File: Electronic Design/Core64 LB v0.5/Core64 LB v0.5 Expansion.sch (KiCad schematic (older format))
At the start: 21 parts, among them J2 HEADER_11-PIN_0.1, J5 HEADER_8-PIN_0.1, J6 HEADER_8-PIN_0.1, U5 74HC238, U8 Adafruit_3.2_TFT_1743, X1 QWIIC, X2 Header_9-PIN_0.1, X3 SAO_conn_SFH11-NBPC-D03-ST-BK, X4 SSW-104-22-L-S-VS

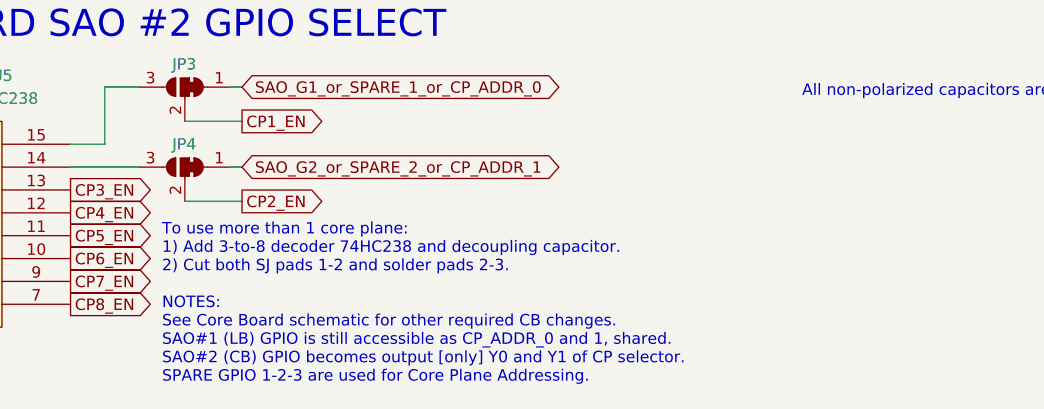
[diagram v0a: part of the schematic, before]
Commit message: Connect row-col-0 to analog inputs for self-test mode
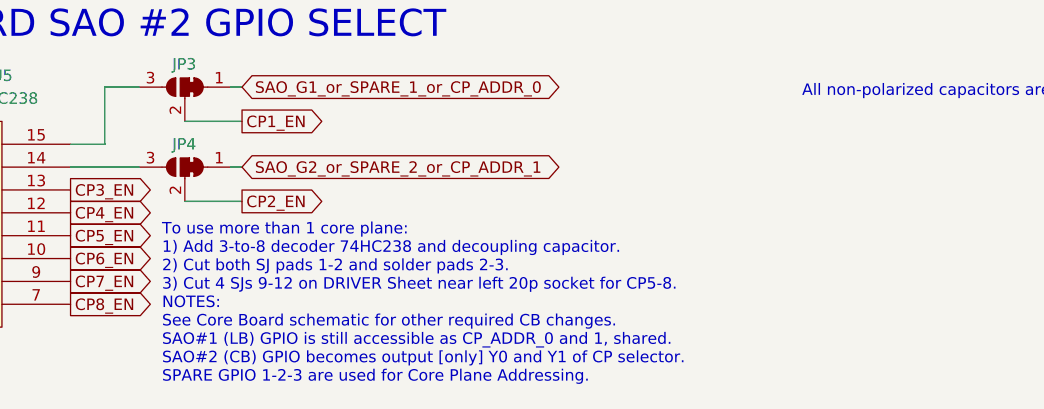
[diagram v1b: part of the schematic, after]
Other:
- note added: "To use more than 1 core plane:\n1) Add 3-to-8 decoder 74HC238 and decoupling capacitor.\n2) Cut both SJ pads 1-2 and solder pads 2-3.\n3) Cut 4 SJs 9-12 on DRIVER Sheet near left 20p socket for CP5-8.\nNOTES:\nSee Core Board schematic for other required CB changes.\nSAO#1 (LB) GPIO is still accessible as CP_ADDR_0 and 1, shared.\nSAO#2 (CB) GPIO becomes output [only] Y0 and Y1 of CP selector.\nSP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"
- note removed: "To use more than 1 core plane:\n1) Add 3-to-8 decoder 74HC238 and decoupling capacitor.\n2) Cut both SJ pads 1-2 and solder pads 2-3.\n\nNOTES:\nSee Core Board schematic for other required CB changes.\nSAO#1 (LB) GPIO is still accessible as CP_ADDR_0 and 1, shared.\nSAO#2 (CB) GPIO becomes output [only] Y0 and Y1 of CP selector.\nSPARE GPIO 1-2-3 are used for Core Plane Addressing."
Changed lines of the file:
@@
 EVERYTHING ON THIS SHEET IS USER-PROVIDED OPTIONAL ADD-ONS
 Text Notes 3500 8000 0    50   ~ 0
-To use more than 1 core plane:\n1) Add 3-to-8 decoder 74HC238 and decoupling capacitor.\n2) Cut both SJ pads 1-2 and solder pads 2-3.\n\nNOTES:\nSee Core Board schematic for other required CB changes.\nSAO#1 (LB) GPIO is still accessible as CP_ADDR_0 and 1, shared.\nSAO#2 (CB) GPIO becomes output [only] Y0 and Y1 of CP selector.\nSPARE GPIO 1-2-3 are used for Core Plane Addressing.
+To use more than 1 core plane:\n1) Add 3-to-8 decoder 74HC238 and decoupling capacitor.\n2) Cut both SJ pads 1-2 and solder pads 2-3.\n3) Cut 4 SJs 9-12 on DRIVER Sheet near left 20p socket for CP5-8.\nNOTES:\nSee Core Board schematic for other required CB changes.\nSAO#1 (LB) GPIO is still accessible as CP_ADDR_0 and 1, shared.\nSAO#2 (CB) GPIO becomes output [only] Y0 and Y1 of CP selector.\nSPARE GPIO 1-2-3 are used for Core Plane Addressing.
 Wire Wire Line
 	3600 6850 3850 6850

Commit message: LB layout redlines
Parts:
- U5: footprint Digikey:TSSOP-16-1EP_W4.40mm -> Digikey:TSSOP-16-W4.40mm
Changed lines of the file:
@@
 F 0 "U5" H 2800 7650 50  0000 C CNN
 F 1 "74HC238" H 2800 7550 50  0000 C CNN
-F 2 "Digikey:TSSOP-16-1EP_W4.40mm" H 2550 7150 50  0001 C CNN
+F 2 "Digikey:TSSOP-16-W4.40mm" H 2550 7150 50  0001 C CNN
 F 3 "" H 2550 7150 50  0001 C CNN
 	1    2550 7150

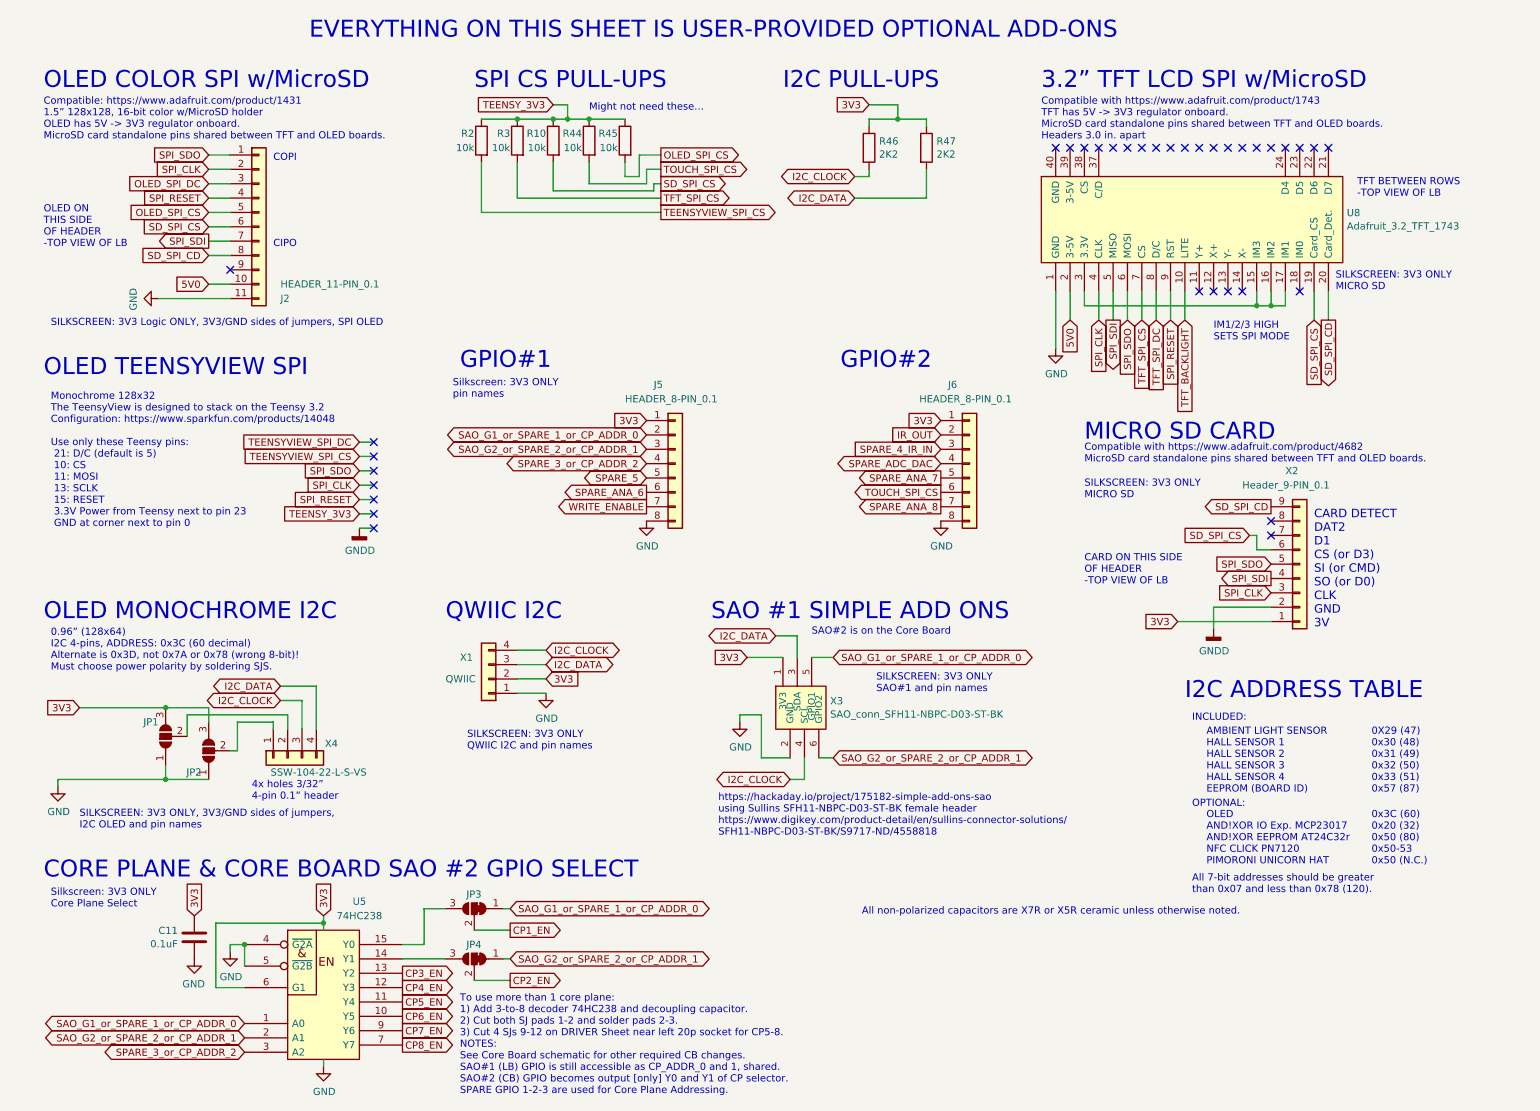
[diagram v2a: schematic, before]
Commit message: Update schematic battery and LiPo charger notes, move SD_CD from ANA_6 to SPARE_3, schematic red lines
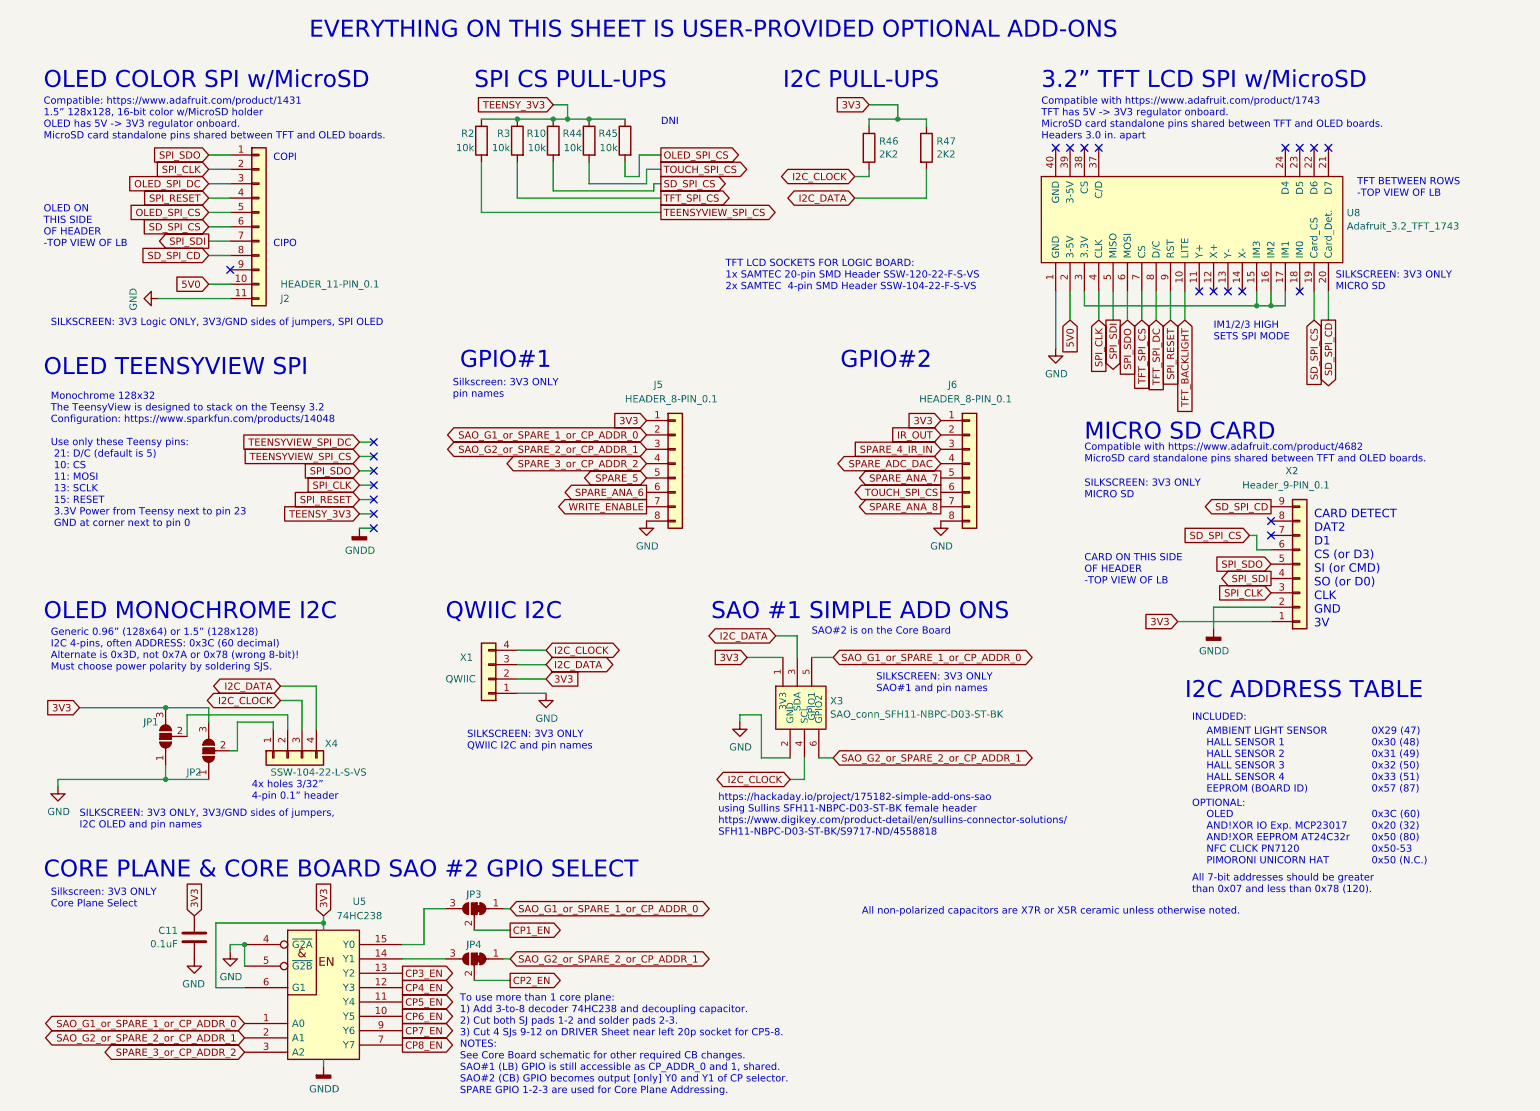
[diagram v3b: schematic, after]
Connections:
- net GNDD is gone; now on net GND: X2.2 (Pin_2)
- no-connect marks 35 -> 23
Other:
- note added: "DNI"
- note added: "Generic 0.96” (128x64) or 1.5” (128x128)\nI2C 4-pins, often ADDRESS: 0x3C (60 decimal)\nAlternate is 0x3D, not 0x7A or 0x78 (wrong 8-bit)!\nMust choose power polarity by soldering SJS."
- note added: "TFT LCD SOCKETS FOR LOGIC BOARD:\n1x SAMTEC 20-pin SMD Header SSW-120-22-F-S-VS\n2x SAMTEC 4-pin SMD Header SSW-104-22-F-S-VS"
- note removed: "0.96” (128x64)\nI2C 4-pins, ADDRESS: 0x3C (60 decimal)\nAlternate is 0x3D, not 0x7A or 0x78 (wrong 8-bit)!\nMust choose power polarity by soldering SJS."
- note removed: "Might not need these…"
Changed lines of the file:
@@
 Date "2021-02-04"
 Rev "0.5"
-Comp "www.Core64.io"
-Comment1 "Work in progress"
-Comment2 "Andy Geppert"
+Comp "Concept and design by Andy Geppert @ www.MachineIdeas.com"
+Comment1 "Visit www.Core64.io for information on assembly and optional features."
+Comment2 "*** Work in progress ***"
 Comment3 ""
-Comment4 ""
+Comment4 "All non-polarized capacitors are X7R or X5R ceramic unless otherwise noted."
 $EndDescr
 Text Notes 600  6500 0    118  ~ 0
@@
 	2200 5400 2200 5450
 Text Notes 650  5050 0    50   ~ 0
-0.96” (128x64)\nI2C 4-pins, ADDRESS: 0x3C (60 decimal)\nAlternate is 0x3D, not 0x7A or 0x78 (wrong 8-bit)!\nMust choose power polarity by soldering SJS.
-$Comp
-L badgelife_shitty_addon_v169bis:SAO_conn_SFH11-NBPC-D03-ST-BK X3
-U 1 1 5E88FF30
-P 5900 5250
-F 0 "X3" H 6079 5247 50  0000 L CNN
-F 1 "SAO_conn_SFH11-NBPC-D03-ST-BK" H 6079 5154 50  0000 L CNN
-F 2 "badgelife_sao_v169bis:Badgelife-SAOv169-BADGE-2x3" H 5900 5450 50  0001 C CNN
-F 3 "" H 5900 5450 50  0001 C CNN
-	1    5900 5250
-	1    0    0    -1
-$EndComp
+Generic 0.96” (128x64) or 1.5” (128x128)\nI2C 4-pins, often ADDRESS: 0x3C (60 decimal)\nAlternate is 0x3D, not 0x7A or 0x78 (wrong 8-bit)!\nMust choose power polarity by soldering SJS.
 Text GLabel 5500 4950 0    50   Input ~ 0
 3V3
@@
 	1    0    0    -1
 $EndComp
-$Comp
-L Connector_Generic:Conn_01x09 X2
-U 1 1 5EAA1F67
-P 9350 4300
-AR Path="/5EA63449/5EAA1F67" Ref="X2"  Part="1"
-AR Path="/5EAA1F67" Ref="X?"  Part="1"
-F 0 "X2" H 9250 3650 50  0000 L CNN
-F 1 "Header_9-PIN_0.1" H 8950 3750 50  0000 L CNN
-F 2 "Connector_PinSocket_2.54mm:PinSocket_1x09_P2.54mm_Vertical" H 9350 4300 50  0001 C CNN
-F 3 "~" H 9350 4300 50  0001 C CNN
-	1    9350 4300
-	1    0    0    1
-$EndComp
 Wire Wire Line
 	8750 4750 8750 4600
@@
 Text Notes 6300 6750 0    50   ~ 0
 All non-polarized capacitors are X7R or X5R ceramic unless otherwise noted.
-$Comp
-L power:GND #PWR?
-U 1 1 5F702794
-P 2550 7800
-AR Path="/5E755787/5F702794" Ref="#PWR?"  Part="1"
-AR Path="/5EA63449/5F702794" Ref="#PWR0126"  Part="1"
-F 0 "#PWR0126" H 2550 7550 50  0001 C CNN
-F 1 "GND" H 2555 7625 50  0000 C CNN
-F 2 "" H 2550 7800 50  0001 C CNN
-F 3 "" H 2550 7800 50  0001 C CNN
-	1    2550 7800
-	1    0    0    -1
-$EndComp
 Text GLabel 2550 6750 1    50   Input ~ 0
 3V3
@@
 Wire Wire Line
 	2000 7100 2000 6950
-Text GLabel 3850 6850 2    50   Output ~ 0
-CP1_EN
 $Comp
 L power:GND #PWR?
@@
 Text GLabel 2000 7600 0    50   BiDi ~ 0
 SAO_G2_or_SPARE_2_or_CP_ADDR_1
-Text GLabel 3850 6700 2    50   BiDi ~ 0
-SAO_G1_or_SPARE_1_or_CP_ADDR_0
 Text GLabel 3850 7050 2    50   BiDi ~ 0
 SAO_G2_or_SPARE_2_or_CP_ADDR_1
@@
 Text Notes 3500 8000 0    50   ~ 0
 To use more than 1 core plane:\n1) Add 3-to-8 decoder 74HC238 and decoupling capacitor.\n2) Cut both SJ pads 1-2 and solder pads 2-3.\n3) Cut 4 SJs 9-12 on DRIVER Sheet near left 20p socket for CP5-8.\nNOTES:\nSee Core Board schematic for other required CB changes.\nSAO#1 (LB) GPIO is still accessible as CP_ADDR_0 and 1, shared.\nSAO#2 (CB) GPIO becomes output [only] Y0 and Y1 of CP selector.\nSPARE GPIO 1-2-3 are used for Core Plane Addressing.
-Wire Wire Line
-	3600 6850 3850 6850
-Wire Wire Line
-	3800 6700 3850 6700
-$Comp
-L Jumper:SolderJumper_3_Bridged12 JP3
-U 1 1 5F5B143C
-P 3600 6700
-F 0 "JP3" H 3550 6800 50  0000 L CNN
-F 1 "SolderJumper_3_Open" V 3200 6250 50  0001 L CNN
-F 2 "Jumper:SolderJumper-3_P1.3mm_Bridged12_RoundedPad1.0x1.5mm_NumberLabels" H 3600 6700 50  0001 C CNN
-F 3 "~" H 3600 6700 50  0001 C CNN
-	1    3600 6700
-	-1   0    0    -1
-$EndComp
 Wire Wire Line
 	3850 7050 3800 7050
@@
 NoConn ~ 7850 1400
 NoConn ~ 7950 1400
-NoConn ~ 8050 1400
-NoConn ~ 8150 1400
-NoConn ~ 8250 1400
-NoConn ~ 8350 1400
-NoConn ~ 8450 1400
-NoConn ~ 8550 1400
-NoConn ~ 8650 1400
-NoConn ~ 8750 1400
-NoConn ~ 8850 1400
-NoConn ~ 8950 1400
-NoConn ~ 9050 1400
-NoConn ~ 9150 1400
 NoConn ~ 9250 1400
 NoConn ~ 9350 1400
@@
 Wire Wire Line
 	6750 1750 6250 1750
-Text Notes 4400 1150 0    50   ~ 0
-Might not need these…
+Text Notes 4900 1250 0    50   ~ 0
+DNI
 Text GLabel 6850 3700 0    50   Output ~ 0
 SPARE_ANA_7
@@
 Text GLabel 4150 1100 0    50   Input ~ 0
 TEENSY_3V3
+$Comp
+L badgelife_shitty_addon_v169bis:SAO_conn_SFH11-NBPC-D03-ST-BK X3
+U 1 1 5E88FF30
+P 5900 5250
+F 0 "X3" H 6079 5247 50  0000 L CNN
+F 1 "SAO_conn_SFH11-NBPC-D03-ST-BK" H 6079 5154 50  0000 L CNN
+F 2 "badgelife_sao_v169bis:Badgelife-SAOv169-BADGE-2x3" H 5900 5450 50  0001 C CNN
+F 3 "" H 5900 5450 50  0001 C CNN
+	1    5900 5250
+	1    0    0    -1
+$EndComp
+$Comp
+L Connector_Generic:Conn_01x09 X2
+U 1 1 5EAA1F67
+P 9350 4300
+AR Path="/5EA63449/5EAA1F67" Ref="X2"  Part="1"
+AR Path="/5EAA1F67" Ref="X?"  Part="1"
+F 0 "X2" H 9250 3650 50  0000 L CNN
+F 1 "Header_9-PIN_0.1" H 8950 3750 50  0000 L CNN
+F 2 "Connector_PinSocket_2.54mm:PinSocket_1x09_P2.54mm_Vertical" H 9350 4300 50  0001 C CNN
+F 3 "~" H 9350 4300 50  0001 C CNN
+	1    9350 4300
+	1    0    0    1
+$EndComp
+Text Notes 5350 2400 0    50   ~ 0
+TFT LCD SOCKETS FOR LOGIC BOARD:\n1x SAMTEC 20-pin SMD Header SSW-120-22-F-S-VS\n2x SAMTEC  4-pin SMD Header SSW-104-22-F-S-VS
+$Comp
+L power:GNDD #PWR0116
+U 1 1 604FF352
+P 2550 7800
+F 0 "#PWR0116" H 2550 7550 50  0001 C CNN
+F 1 "GNDD" H 2555 7644 50  0000 C CNN
+F 2 "" H 2550 7800 50  0001 C CNN
+F 3 "" H 2550 7800 50  0001 C CNN
+	1    2550 7800
+	1    0    0    -1
+$EndComp
+$Comp
+L Jumper:SolderJumper_3_Bridged12 JP3
+U 1 1 5F5B143C
+P 3600 6700
+F 0 "JP3" H 3550 6800 50  0000 L CNN
+F 1 "SolderJumper_3_Open" V 3200 6250 50  0001 L CNN
+F 2 "Jumper:SolderJumper-3_P1.3mm_Bridged12_RoundedPad1.0x1.5mm_NumberLabels" H 3600 6700 50  0001 C CNN
+F 3 "~" H 3600 6700 50  0001 C CNN
+	1    3600 6700
+	-1   0    0    -1
+$EndComp
+Wire Wire Line
+	3800 6700 3850 6700
+Wire Wire Line
+	3600 6850 3850 6850
+Text GLabel 3850 6700 2    50   BiDi ~ 0
+SAO_G1_or_SPARE_1_or_CP_ADDR_0
+Text GLabel 3850 6850 2    50   Output ~ 0
+CP1_EN
 $EndSCHEMATC

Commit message: Refine and release LB and CB V0.5 layout for prototyping
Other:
- note added: "OLED SOCKET FOR LOGIC BOARD:\nSAMTEC 4-pin SMD Header SSW-104-22-F-S-VS"
- note removed: "All non-polarized capacitors are X7R or X5R ceramic unless otherwise noted."
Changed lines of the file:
@@
 Sheet 3 5
 Title "Core 64 - Expansion"
-Date "2021-02-04"
+Date "2021-02-27"
 Rev "0.5"
 Comp "Concept and design by Andy Geppert @ www.MachineIdeas.com"
 Comment1 "Visit www.Core64.io for information on assembly and optional features."
-Comment2 "*** Work in progress ***"
+Comment2 "*** As prototyped. ***"
 Comment3 ""
 Comment4 "All non-polarized capacitors are X7R or X5R ceramic unless otherwise noted."
@@
 Text Notes 3450 3150 0    50   ~ 0
 Silkscreen: 3V3 ONLY\npin names
-Text Notes 6300 6750 0    50   ~ 0
-All non-polarized capacitors are X7R or X5R ceramic unless otherwise noted.
 Text GLabel 2550 6750 1    50   Input ~ 0
 3V3
@@
 Text GLabel 3850 6850 2    50   Output ~ 0
 CP1_EN
+Text Notes 650  4500 0    50   ~ 0
+OLED SOCKET FOR LOGIC BOARD:\nSAMTEC 4-pin SMD Header SSW-104-22-F-S-VS
 $EndSCHEMATC
